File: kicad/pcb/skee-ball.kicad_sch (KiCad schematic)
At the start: 62 parts, among them J13 HEADER, J18 DC_DRIVER, J19 JOYSTICK, J2 EXTERNAL_BUTTON, J20 SERVO, J21 US0, J22 US1, J26 US2, J27 US3, J3 NHD_CONN1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

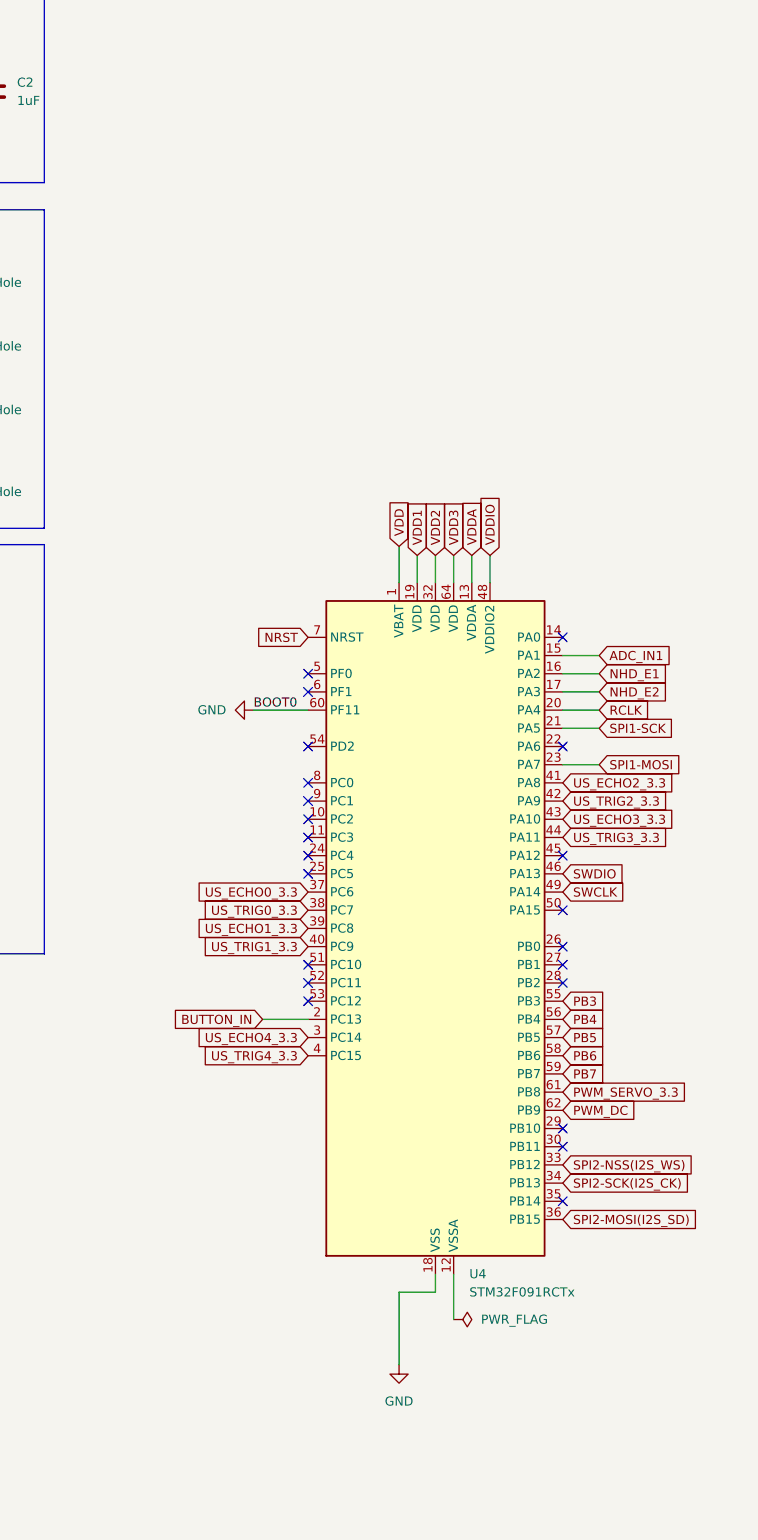
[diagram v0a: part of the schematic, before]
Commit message: update schematic sheet details
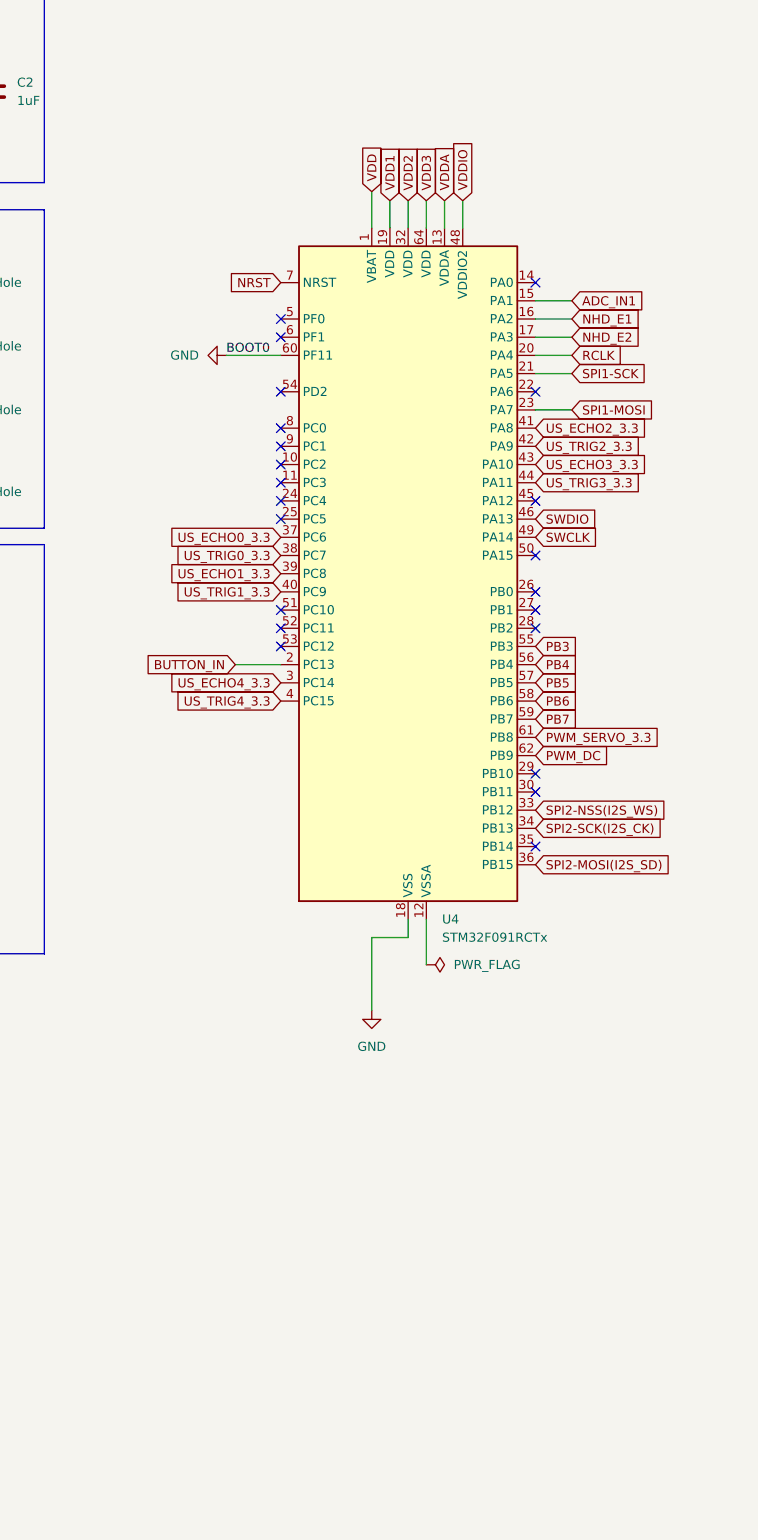
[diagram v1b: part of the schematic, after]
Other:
- company: Team 1 -> Purdue University
- moved on the sheet: U4

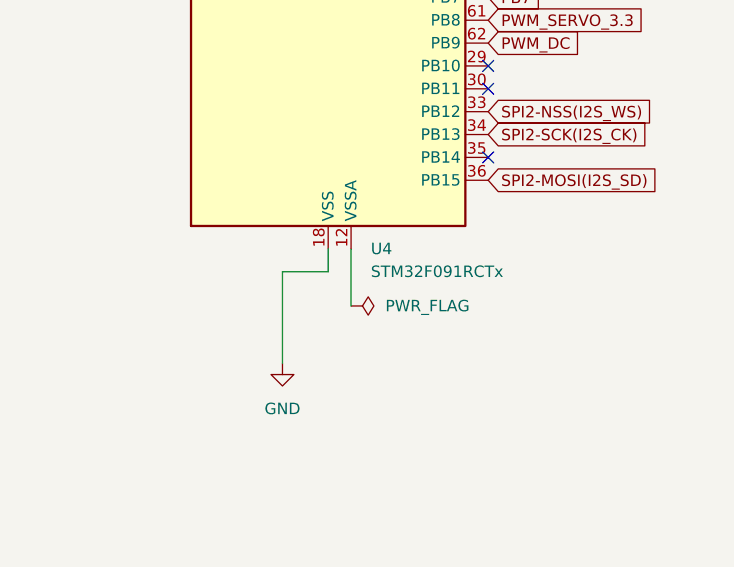
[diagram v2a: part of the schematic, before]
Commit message: fix analog ground plane connection:
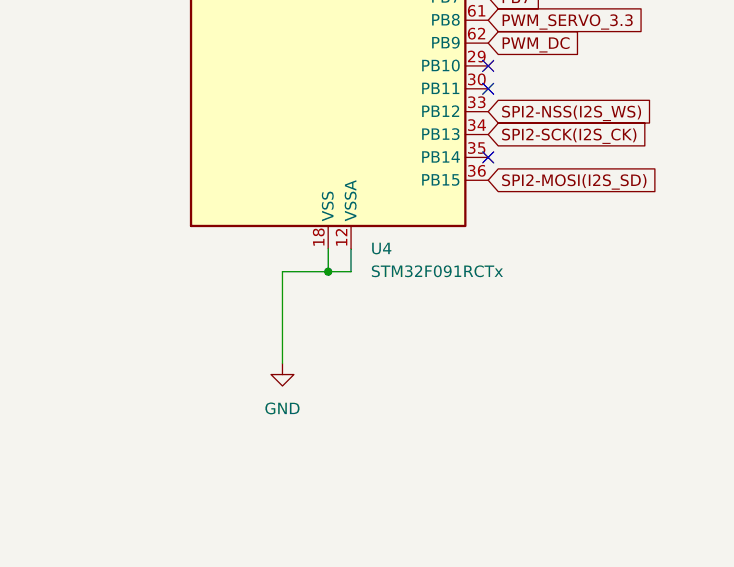
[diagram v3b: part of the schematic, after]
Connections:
- net GND: now also U4.12 (VSSA)
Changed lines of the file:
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@@
 	)
 	(junction
+		(at 358.14 182.88)
+		(diameter 0)
+		(color 0 0 0 0)
+	)
+	(junction
 		(at 242.57 38.1)
 		(diameter 0)
@@
 	(wire
 		(pts
-			(xy 360.68 180.34) (xy 360.68 186.69)
-		)
-		(stroke
-			(width 0)
-			(type default)
-		)
-	)
-	(wire
-		(pts
 			(xy 120.65 227.33) (xy 123.19 227.33)
 		)
@@
 	(wire
 		(pts
+			(xy 360.68 180.34) (xy 360.68 182.88)
+		)
+		(stroke
+			(width 0)
+			(type default)
+		)
+	)
+	(wire
+		(pts
 			(xy 248.92 36.83) (xy 248.92 38.1)
 		)
@@
 	(wire
 		(pts
+			(xy 360.68 182.88) (xy 358.14 182.88)
+		)
+		(stroke
+			(width 0)
+			(type default)
+		)
+	)
+	(wire
+		(pts
 			(xy 35.56 146.05) (xy 38.1 146.05)
 		)
@@
 					(unit 1)
 				)
-			)
-		)
-	)
-	(symbol
-		(lib_id "power:PWR_FLAG")
-		(at 360.68 186.69 270)
-		(unit 1)
-		(exclude_from_sim no)
-		(in_bom yes)
-		(on_board yes)
-		(dnp no)
-		(fields_autoplaced yes)
-		(property "Reference" "#FLG05"
-			(at 362.585 186.69 0)
-			(effects
-				(font
-					(size 1.27 1.27)
-				)
-				(hide yes)
-			)
-		)
-		(property "Value" "PWR_FLAG"
-			(at 364.49 186.6899 90)
-			(effects
-				(font
-					(size 1.27 1.27)
-				)
-				(justify left)
-			)
-		)
-		(property "Footprint" ""
-			(at 360.68 186.69 0)
-			(effects
-				(font
-					(size 1.27 1.27)
-				)
-				(hide yes)
-			)
-		)
-		(property "Datasheet" "~"
-			(at 360.68 186.69 0)
-			(effects
-				(font
-					(size 1.27 1.27)
-				)
-				(hide yes)
-			)
-		)
-		(property "Description" "Special symbol for telling ERC where power comes from"
-			(at 360.68 186.69 0)
-			(effects
-				(font
-					(size 1.27 1.27)
-				)
-				(hide yes)
-			)
-		)
-		(pin "1"
-		)
-		(instances
-			(project ""
-				(path "/547d9dcb-6f5f-42b4-90d7-bfc006b86b9a"
-					(reference "#FLG05")
-					(unit 1)
-				)

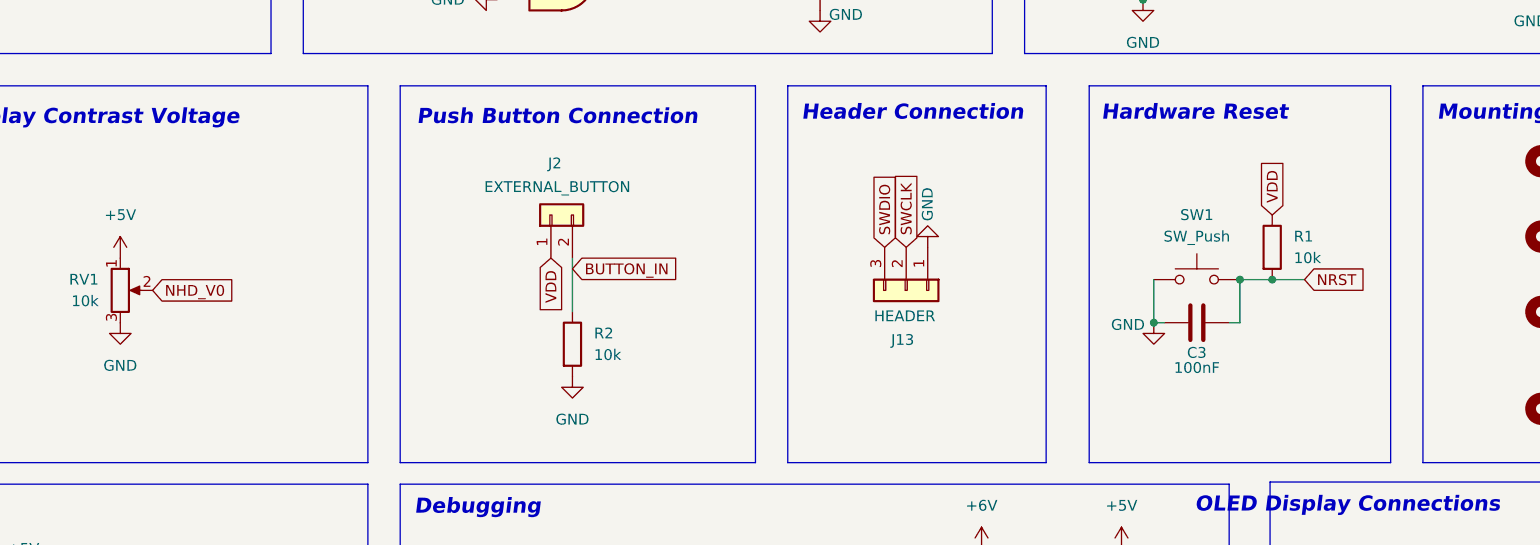
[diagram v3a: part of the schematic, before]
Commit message: add esd protection to pcb
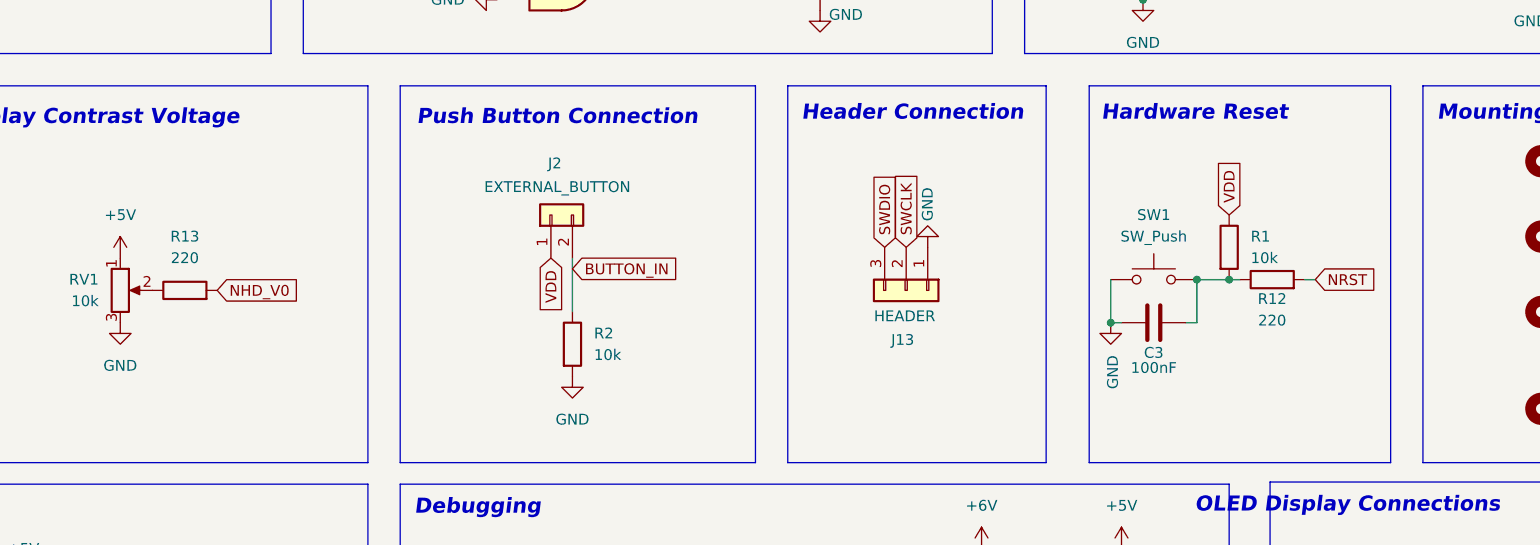
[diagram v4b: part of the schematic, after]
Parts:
- added R12, R13: 220, Resistor_SMD:R_0805_2012Metric_Pad1.20x1.40mm_HandSolder, symbol Device:R
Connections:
- net NHD_V0: now also R13.2; no longer RV1.2
- net NRST: now also R12.2; no longer C3.2, R1.2, SW1.2
- new net: C3.2, R1.2, R12.1, SW1.2
- new net: R13.1, RV1.2
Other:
- moved on the sheet: C3, R1, SW1
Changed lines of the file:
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@@
 	)
 	(junction
+		(at 252.73 104.14)
+		(diameter 0)
+		(color 0 0 0 0)
+	)
+	(junction
 		(at 58.42 116.84)
 		(diameter 0)
@@
 	)
 	(junction
-		(at 254 104.14)
+		(at 248.92 104.14)
 		(diameter 0)
 		(color 0 0 0 0)
@@
 	)
 	(junction
-		(at 243.84 109.22)
-		(diameter 0)
-		(color 0 0 0 0)
-	)
-	(junction
-		(at 257.81 104.14)
+		(at 238.76 109.22)
 		(diameter 0)
 		(color 0 0 0 0)
@@
 	(wire
 		(pts
+			(xy 261.62 104.14) (xy 262.89 104.14)
+		)
+		(stroke
+			(width 0)
+			(type default)
+		)
+	)
+	(wire
+		(pts
 			(xy 50.8 236.22) (xy 50.8 238.76)
 		)
@@
 	(wire
 		(pts
-			(xy 254 104.14) (xy 257.81 104.14)
+			(xy 248.92 104.14) (xy 252.73 104.14)
 		)
 		(stroke
@@
 	(wire
 		(pts
+			(xy 252.73 104.14) (xy 254 104.14)
+		)
+		(stroke
+			(width 0)
+			(type default)
+		)
+	)
+	(wire
+		(pts
 			(xy 118.11 45.72) (xy 130.81 45.72)
 		)
@@
 	(wire
 		(pts
-			(xy 254 109.22) (xy 252.73 109.22)
+			(xy 248.92 109.22) (xy 247.65 109.22)
 		)
 		(stroke
@@
 	(wire
 		(pts
-			(xy 243.84 109.22) (xy 245.11 109.22)
+			(xy 238.76 109.22) (xy 240.03 109.22)
 		)
 		(stroke
@@
 	(wire
 		(pts
-			(xy 254 104.14) (xy 254 109.22)
+			(xy 248.92 104.14) (xy 248.92 109.22)
 		)
 		(stroke
@@
 	(wire
 		(pts
-			(xy 257.81 104.14) (xy 261.62 104.14)
-		)
-		(stroke
-			(width 0)
-			(type default)
-		)
-	)
-	(wire
-		(pts
 			(xy 360.68 180.34) (xy 360.68 182.88)
 		)
@@
 	(wire
 		(pts
-			(xy 243.84 104.14) (xy 243.84 109.22)
+			(xy 238.76 104.14) (xy 238.76 109.22)
 		)
 		(stroke
@@
 	(label "BOOT0"
 		(at 332.74 101.6 0)
+		(fields_autoplaced yes)
 		(effects
 			(font
@@
 	(global_label "NRST"
 		(shape input)
-		(at 261.62 104.14 0)
+		(at 262.89 104.14 0)
 		(fields_autoplaced yes)
 		(effects
@@
 		)
 		(property "Intersheetrefs" "${INTERSHEET_REFS}"
-			(at 269.3828 104.14 0)
+			(at 270.6528 104.14 0)
 			(effects
 				(font
@@
 	(global_label "VDD"
 		(shape input)
-		(at 257.81 96.52 90)
+		(at 252.73 96.52 90)
 		(fields_autoplaced yes)
 		(effects
@@
 		)
 		(property "Intersheetrefs" "${INTERSHEET_REFS}"
-			(at 257.81 89.9062 90)
+			(at 252.73 89.9062 90)
 			(effects
 				(font
@@
 	(global_label "NHD_V0"
 		(shape input)
-		(at 125.73 105.41 0)
+		(at 133.35 105.41 0)
 		(fields_autoplaced yes)
 		(effects
@@
 		)
 		(property "Intersheetrefs" "${INTERSHEET_REFS}"
-			(at 135.9119 105.41 0)
+			(at 143.5319 105.41 0)
 			(effects
 				(font
@@
 	(symbol
 		(lib_id "Switch:SW_Push")
-		(at 248.92 104.14 0)
+		(at 243.84 104.14 0)
 		(unit 1)
 		(exclude_from_sim no)
@@
 		(fields_autoplaced yes)
 		(property "Reference" "SW1"
-			(at 248.92 96.52 0)
+			(at 243.84 96.52 0)
 			(effects
 				(font
@@
 		)
 		(property "Value" "SW_Push"
-			(at 248.92 99.06 0)
+			(at 243.84 99.06 0)
 			(effects
 				(font
@@
 		)
 		(property "Footprint" "Button_Switch_THT:SW_PUSH_6mm"
-			(at 248.92 99.06 0)
+			(at 243.84 99.06 0)
 			(effects
 				(font
@@
 		)
 		(property "Datasheet" "~"
-			(at 248.92 99.06 0)
+			(at 243.84 99.06 0)
 			(effects
 				(font
@@
 		)
 		(property "Description" "Push button switch, generic, two pins"
-			(at 248.92 104.14 0)
+			(at 243.84 104.14 0)
 			(effects
 				(font
@@
 	(symbol
 		(lib_id "Device:C")
-		(at 248.92 109.22 90)
+		(at 243.84 109.22 90)
 		(unit 1)
 		(exclude_from_sim no)
@@
 		(dnp no)
 		(property "Reference" "C3"
-			(at 248.92 112.776 90)
+			(at 243.84 112.776 90)
 			(effects
 				(font
@@
 		)
 		(property "Value" "100nF"
-			(at 248.92 114.554 90)
+			(at 243.84 114.554 90)
 			(effects
 				(font
@@
 		)
 		(property "Footprint" "Capacitor_SMD:C_0805_2012Metric_Pad1.18x1.45mm_HandSolder"
-			(at 252.73 108.2548 0)
+			(at 247.65 108.2548 0)
 			(effects
 				(font
@@
 		)
 		(property "Datasheet" "~"
-			(at 248.92 109.22 0)
+			(at 243.84 109.22 0)
 			(effects
 				(font
@@
 		)
 		(property "Description" "Unpolarized capacitor"
-			(at 248.92 109.22 0)
+			(at 243.84 109.22 0)
 			(effects
 				(font
@@
 	(symbol
 		(lib_id "power:GND")
-		(at 243.84 109.22 0)
+		(at 238.76 109.22 0)
 		(unit 1)
 		(exclude_from_sim no)
@@
 		(dnp no)
 		(property "Reference" "#PWR066"
-			(at 243.84 115.57 0)
+			(at 238.76 115.57 0)
 			(effects
 				(font
@@
 		)
 		(property "Value" "GND"
-			(at 240.792 109.474 0)
+			(at 239.014 115.062 90)
 			(effects
 				(font
@@
 		)
 		(property "Footprint" ""
-			(at 243.84 109.22 0)
+			(at 238.76 109.22 0)
 			(effects
 				(font
@@
 		)
 		(property "Datasheet" ""
-			(at 243.84 109.22 0)
+			(at 238.76 109.22 0)
 			(effects
 				(font
@@
 		)
 		(property "Description" "Power symbol creates a global label with name \"GND\" , ground"
-			(at 243.84 109.22 0)
+			(at 238.76 109.22 0)
 			(effects
 				(font
@@
 	(symbol
 		(lib_id "Device:R")
-		(at 257.81 100.33 0)
+		(at 252.73 100.33 0)
 		(unit 1)
 		(exclude_from_sim no)
@@
 		(fields_autoplaced yes)
 		(property "Reference" "R1"
-			(at 260.35 99.0599 0)
+			(at 255.27 99.0599 0)
 			(effects
 				(font
@@
 		)
 		(property "Value" "10k"
-			(at 260.35 101.5999 0)
+			(at 255.27 101.5999 0)
 			(effects
 				(font
@@
 		)
 		(property "Footprint" "Resistor_SMD:R_0805_2012Metric_Pad1.20x1.40mm_HandSolder"
-			(at 256.032 100.33 90)
+			(at 250.952 100.33 90)
 			(effects
 				(font
@@
 		)
 		(property "Datasheet" "~"
-			(at 257.81 100.33 0)
+			(at 252.73 100.33 0)
 			(effects
 				(font
@@
 		)
 		(property "Description" "Resistor"
-			(at 257.81 100.33 0)
+			(at 252.73 100.33 0)
 			(effects
 				(font
@@
 	)
 	(symbol
+		(lib_id "Device:R")
+		(at 257.81 104.14 90)
+		(unit 1)
+		(exclude_from_sim no)
+		(in_bom yes)
+		(on_board yes)
+		(dnp no)
+		(property "Reference" "R12"
+			(at 257.81 106.426 90)
+			(effects
+				(font
+					(size 1.27 1.27)
+				)
+			)
+		)
+		(property "Value" "220"
+			(at 257.81 108.966 90)
+			(effects
+				(font
+					(size 1.27 1.27)
+				)
+			)
+		)
+		(property "Footprint" "Resistor_SMD:R_0805_2012Metric_Pad1.20x1.40mm_HandSolder"
+			(at 257.81 105.918 90)
+			(effects
+				(font
+					(size 1.27 1.27)
+				)
+				(hide yes)
+			)
+		)
+		(property "Datasheet" "~"
+			(at 257.81 104.14 0)
+			(effects
+				(font
+					(size 1.27 1.27)
+				)
+				(hide yes)
+			)
+		)
+		(property "Description" "Resistor"
+			(at 257.81 104.14 0)
+			(effects
+				(font
+					(size 1.27 1.27)
+				)
+				(hide yes)
+			)
+		)
+		(pin "2"
+		)
+		(pin "1"
+		)
+		(instances
+			(project ""
+				(path "/547d9dcb-6f5f-42b4-90d7-bfc006b86b9a"
+					(reference "R12")
+					(unit 1)
+				)
+			)
+		)
+	)
+	(symbol
 		(lib_id "power:+5V")
 		(at 195.58 205.74 270)
@@
 					(unit 1)
 				)
+			)
+		)
+	)
+	(symbol
+		(lib_id "Device:R")
+		(at 129.54 105.41 90)
+		(unit 1)
+		(exclude_from_sim no)
+		(in_bom yes)
+		(on_board yes)
+		(dnp no)
+		(fields_autoplaced yes)
+		(property "Reference" "R13"
+			(at 129.54 99.06 90)
+			(effects
+				(font
+					(size 1.27 1.27)
+				)
+			)
+		)
+		(property "Value" "220"
+			(at 129.54 101.6 90)
+			(effects
+				(font
+					(size 1.27 1.27)
+				)
+			)
+		)
+		(property "Footprint" "Resistor_SMD:R_0805_2012Metric_Pad1.20x1.40mm_HandSolder"
+			(at 129.54 107.188 90)
+			(effects
+				(font
+					(size 1.27 1.27)
+				)
+				(hide yes)
+			)
+		)
+		(property "Datasheet" "~"
+			(at 129.54 105.41 0)
+			(effects
+				(font
+					(size 1.27 1.27)
+				)
+				(hide yes)
+			)
+		)
+		(property "Description" "Resistor"
+			(at 129.54 105.41 0)
+			(effects
+				(font
+					(size 1.27 1.27)
+				)
+				(hide yes)
+			)
+		)
+		(pin "2"
+		)
+		(pin "1"
+		)
+		(instances
+			(project ""
+				(path "/547d9dcb-6f5f-42b4-90d7-bfc006b86b9a"
+					(reference "R13")
+					(unit 1)
+				)

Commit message: pcb revisions before approval
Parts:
- added R14, R15: 220, Resistor_SMD:R_0805_2012Metric_Pad1.20x1.40mm_HandSolder, symbol Device:R
- added R16: 2200, Resistor_SMD:R_0805_2012Metric_Pad1.20x1.40mm_HandSolder, symbol Device:R
- added U11: MAX7375AXR805, Package_TO_SOT_SMD:SOT-323_SC-70, symbol Oscillator:MAX7375AXR805
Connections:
- net ADC_IN1: now also R14.2; no longer J19.3 (Pin_3)
- net BUTTON_IN: now also R15.2; no longer J2.2 (Pin_2), R2.1
- net GND: now also R16.1, U11.3 (GND); no longer U4.60 (PF11)
- net VDD: now also U11.1 (V+)
- net EXTERNAL_CLK: now reaches U4.5 (PF0)
- net EXTERNAL_CLK: now also U11.2 (CLOCK)
- new net: J2.2 (Pin_2), R15.1, R2.1
- new net: J19.3 (Pin_3), R14.1
- new net BOOT0: R16.2, U4.60 (PF11)
- no-connect marks 46 -> 45
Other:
- note added: "External Oscillator"
- note added: "Ultrasonic Sensor Connections"
- moved on the sheet: J19
